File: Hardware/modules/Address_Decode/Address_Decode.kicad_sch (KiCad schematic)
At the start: 28 parts, among them J1 Bus_PCI_6502, J2 Clock_Sel, J3 Conn_01x08, SW1 Manual_Clock, U1 74HC14, U2 74HC00, U3 74LS20, U4 DS1501YZ, U5 74LS393, U6 74HC138, U7 74HC688, X1 8MHz, Y1 G33270007

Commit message: Big Hardware Update
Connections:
- net PORT_144: now also U2.9
- net PORT_160: no longer U2.9
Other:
- note added: "Address PORT 144@16 -> BF90 - BF9F"
- note removed: "Address PORT 160@16 -> BFA0 - BFAF"
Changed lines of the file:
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@@
 		)
 	)
-	(text "Address PORT 160@16\n-> BFA0 - BFAF"
+	(text "Address PORT 144@16\n-> BF90 - BF9F"
 		(exclude_from_sim no)
 		(at 178.562 28.194 0)
@@
 	)
 	(label "PORT_144"
+		(at 201.93 73.66 180)
+		(fields_autoplaced yes)
+		(effects
+			(font
+				(size 1.27 1.27)
+			)
+			(justify right bottom)
+		)
+	)
+	(label "PORT_144"
 		(at 199.39 106.68 0)
 		(fields_autoplaced yes)
@@
 		)
 	)
-	(label "PORT_160"
-		(at 201.93 73.66 180)
-		(fields_autoplaced yes)
-		(effects
-			(font
-				(size 1.27 1.27)
-			)
-			(justify right bottom)
-		)
-	)

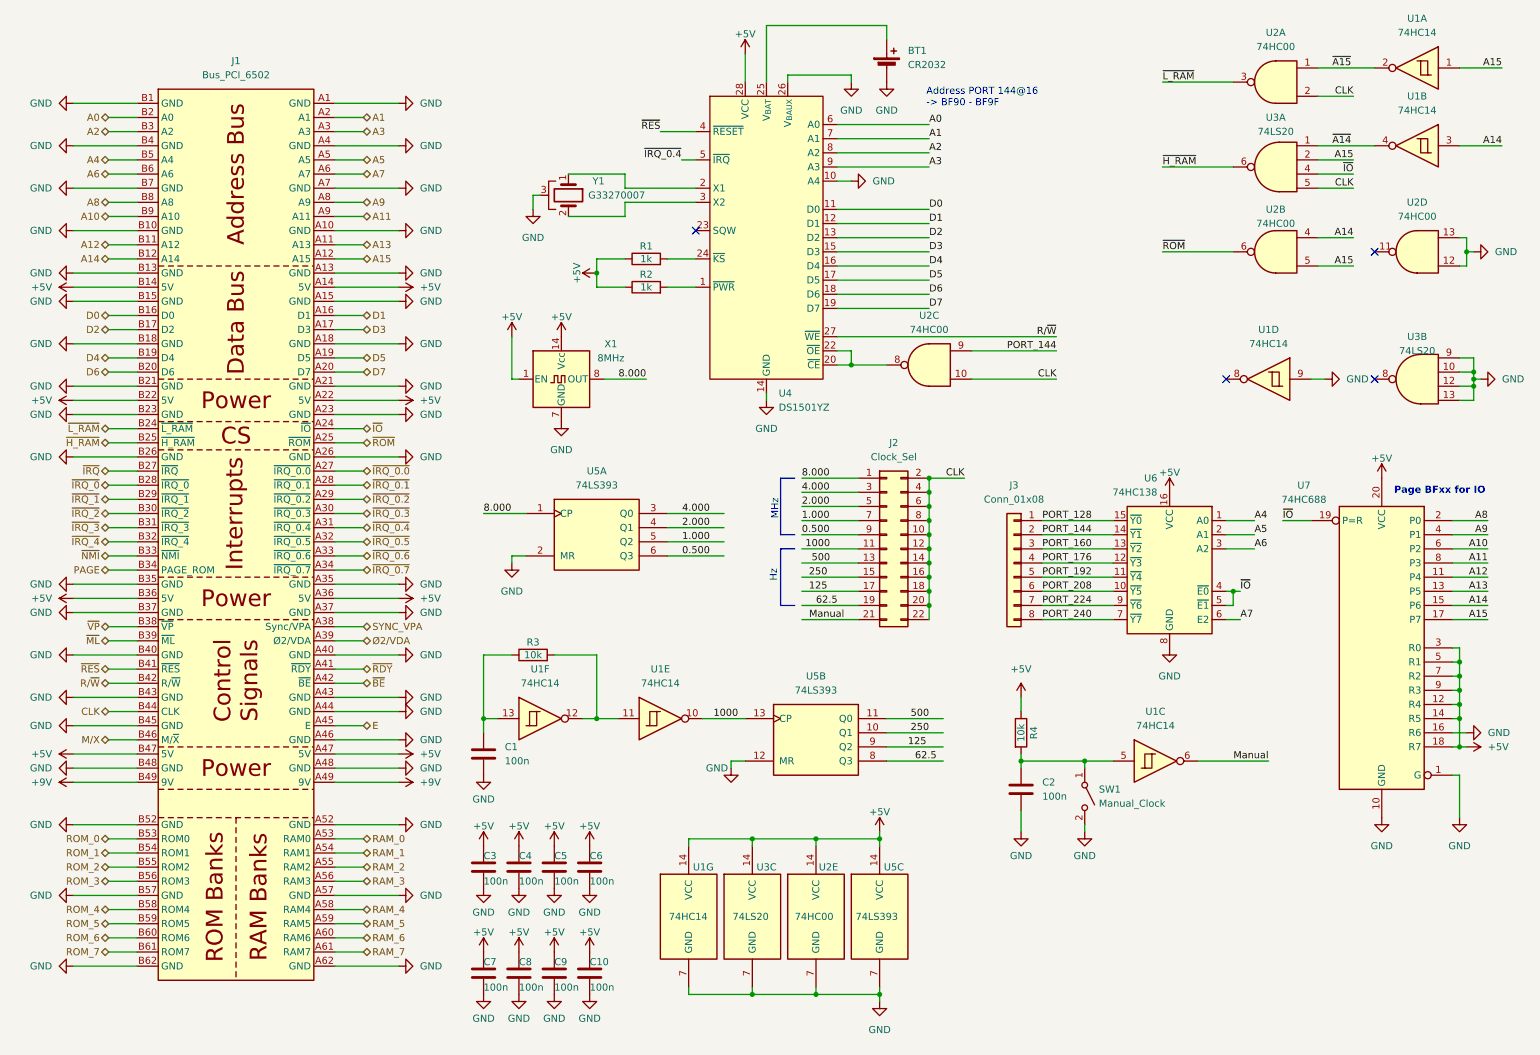
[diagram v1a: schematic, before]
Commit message: Hardware Update Add MyCPU VGA Module Beautify all Schematics minor Error corrections Readme Update
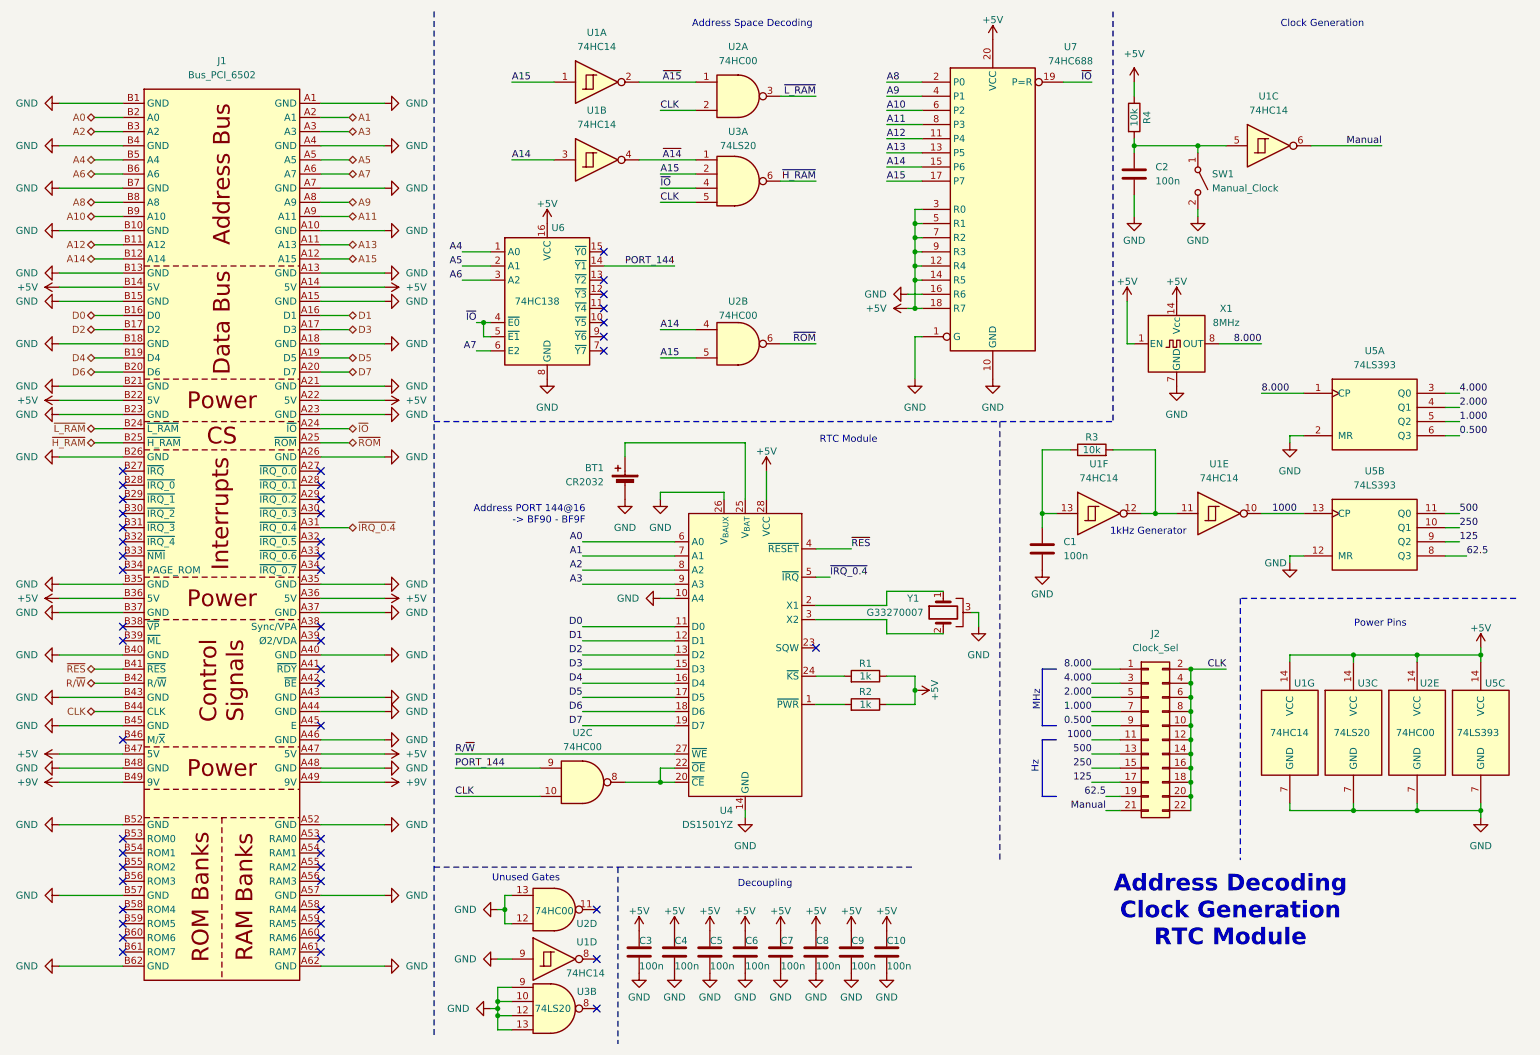
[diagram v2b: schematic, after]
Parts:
- removed J3: Conn_01x08, Connector_PinHeader_2.54mm:PinHeader_1x08_P2.54mm_Vertical, symbol Connector_Generic:Conn_01x08
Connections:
- net E: no longer names the net of J1.A45 (E)
- net M/X: no longer names the net of J1.B46 (M/~{X})
- net PAGE: no longer names the net of J1.B34 (PAGE_ROM)
- net PORT_128: no longer names the net of U6.15 (~{Y0})
- net PORT_160: no longer names the net of U6.13 (~{Y2})
- net PORT_176: no longer names the net of U6.12 (~{Y3})
- net PORT_192: no longer names the net of U6.11 (~{Y4})
- net PORT_208: no longer names the net of U6.10 (~{Y5})
- net PORT_224: no longer names the net of U6.9 (~{Y6})
- net PORT_240: no longer names the net of U6.7 (~{Y7})
- net RAM_0: no longer names the net of J1.A53 (RAM0)
- net RAM_1: no longer names the net of J1.A54 (RAM1)
- net RAM_2: no longer names the net of J1.A55 (RAM2)
- net RAM_3: no longer names the net of J1.A56 (RAM3)
- net RAM_4: no longer names the net of J1.A58 (RAM4)
- net RAM_5: no longer names the net of J1.A59 (RAM5)
- net RAM_6: no longer names the net of J1.A60 (RAM6)
- net RAM_7: no longer names the net of J1.A61 (RAM7)
- net ROM_0: no longer names the net of J1.B53 (ROM0)
- net ROM_1: no longer names the net of J1.B54 (ROM1)
- net ROM_2: no longer names the net of J1.B55 (ROM2)
- net ROM_3: no longer names the net of J1.B56 (ROM3)
- net ROM_4: no longer names the net of J1.B58 (ROM4)
- net ROM_5: no longer names the net of J1.B59 (ROM5)
- net ROM_6: no longer names the net of J1.B60 (ROM6)
- net ROM_7: no longer names the net of J1.B61 (ROM7)
- net SYNC_VPA: no longer names the net of J1.A38 (Sync/VPA)
- net ~{BE}: no longer names the net of J1.A42 (~{BE})
- net ~{IRQ_0.0}: no longer names the net of J1.A27 (~{IRQ_0.0})
- net ~{IRQ_0.1}: no longer names the net of J1.A28 (~{IRQ_0.1})
- net ~{IRQ_0.2}: no longer names the net of J1.A29 (~{IRQ_0.2})
- net ~{IRQ_0.3}: no longer names the net of J1.A30 (~{IRQ_0.3})
- net ~{IRQ_0.5}: no longer names the net of J1.A32 (~{IRQ_0.5})
- net ~{IRQ_0.6}: no longer names the net of J1.A33 (~{IRQ_0.6})
- net ~{IRQ_0.7}: no longer names the net of J1.A34 (~{IRQ_0.7})
- net ~{IRQ_0}: no longer names the net of J1.B28 (~{IRQ_0})
- net ~{IRQ_1}: no longer names the net of J1.B29 (~{IRQ_1})
- net ~{IRQ_2}: no longer names the net of J1.B30 (~{IRQ_2})
- net ~{IRQ_3}: no longer names the net of J1.B31 (~{IRQ_3})
- net ~{IRQ_4}: no longer names the net of J1.B32 (~{IRQ_4})
- net ~{IRQ}: no longer names the net of J1.B27 (~{IRQ})
- net ~{ML}: no longer names the net of J1.B39 (~{ML})
- net ~{NMI}: no longer names the net of J1.B33 (~{NMI})
- net ~{RDY}: no longer names the net of J1.A41 (~{RDY})
- net ~{VP}: no longer names the net of J1.B38 (~{VP})
- net Ø2/VDA: no longer names the net of J1.A39 (Ø2/VDA)
- no-connect marks 4 -> 50
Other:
- note added: "1kHz Generator"
- note added: "Address Decoding Clock Generation RTC Module"
- note added: "Address Space Decoding"
- note added: "Clock Generation"
- note added: "Decoupling"
- note added: "Power Pins"
- note added: "RTC Module"
- note added: "Unused Gates"
- note removed: "Page BFxx for IO"
- company: (none) -> Synthron
- title: (none) -> S65xx Computer System
- moved on the sheet: BT1, C1, C10, C2, C3, C4, C5, C6, C7, C8, C9, J1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

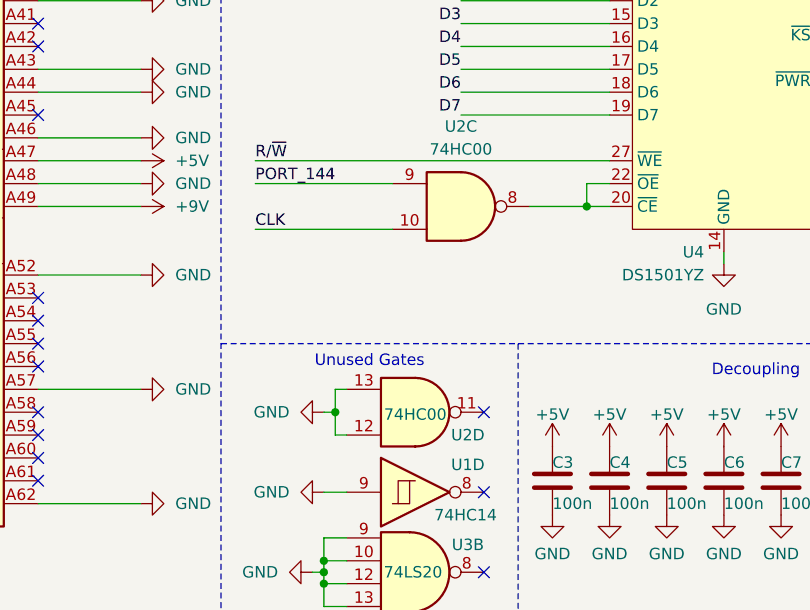
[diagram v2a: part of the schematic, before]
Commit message: Chip Select Strobe Generation Bugfix
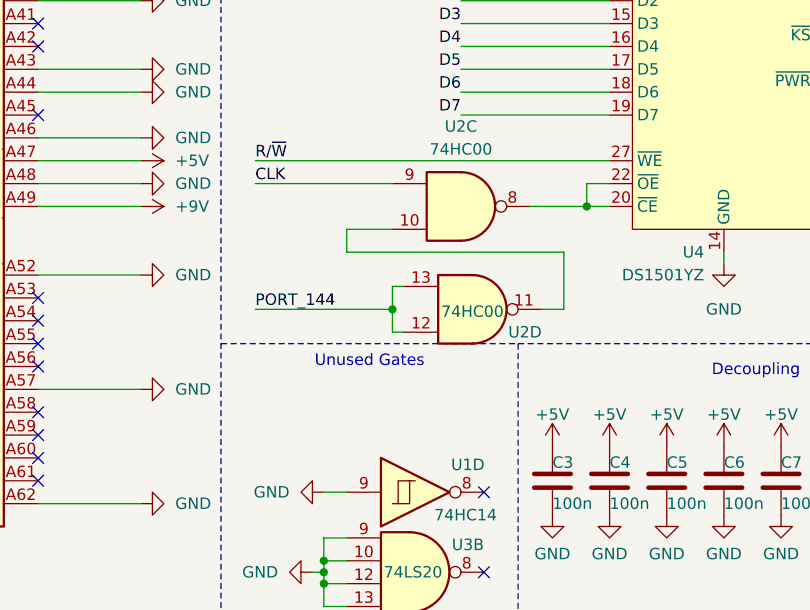
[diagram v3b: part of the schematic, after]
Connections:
- net CLK: now also U2.9; no longer U2.10
- net GND: no longer U2.12, U2.13
- net PORT_144: now also U2.12, U2.13; no longer U2.9
- net at U2.11: now also U2.10
- no-connect marks 50 -> 49
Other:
- moved on the sheet: U2D
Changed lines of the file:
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@@
 	)
 	(junction
-		(at 102.87 173.99)
+		(at 176.53 55.88)
 		(diameter 0)
 		(color 0 0 0 0)
 	)
 	(junction
-		(at 176.53 55.88)
+		(at 99.06 68.58)
 		(diameter 0)
 		(color 0 0 0 0)
 	)
 	(junction
-		(at 99.06 68.58)
+		(at 109.22 162.56)
 		(diameter 0)
 		(color 0 0 0 0)
@@
 	)
 	(no_connect
-		(at 119.38 173.99)
-	)
-	(no_connect
 		(at 120.65 73.66)
 	)
@@
 	(wire
 		(pts
-			(xy 102.87 173.99) (xy 102.87 176.53)
+			(xy 208.28 148.59) (xy 213.36 148.59)
 		)
 		(stroke
@@
 	(wire
 		(pts
-			(xy 208.28 148.59) (xy 213.36 148.59)
+			(xy 171.45 35.56) (xy 177.8 35.56)
 		)
 		(stroke
@@
 	(wire
 		(pts
-			(xy 171.45 35.56) (xy 177.8 35.56)
+			(xy 22.86 140.97) (xy 34.29 140.97)
 		)
 		(stroke
@@
 	(wire
 		(pts
-			(xy 22.86 140.97) (xy 34.29 140.97)
+			(xy 81.28 148.59) (xy 69.85 148.59)
 		)
 		(stroke
@@
 	(wire
 		(pts
-			(xy 81.28 148.59) (xy 69.85 148.59)
+			(xy 104.14 193.04) (xy 101.6 193.04)
 		)
 		(stroke
@@
 	(wire
 		(pts
-			(xy 104.14 193.04) (xy 101.6 193.04)
+			(xy 109.22 162.56) (xy 109.22 160.02)
 		)
 		(stroke
@@
 	(wire
 		(pts
+			(xy 104.14 156.21) (xy 104.14 153.67)
+		)
+		(stroke
+			(width 0)
+			(type default)
+		)
+	)
+	(wire
+		(pts
 			(xy 255.27 128.27) (xy 243.84 128.27)
 		)
@@
 	(wire
 		(pts
-			(xy 102.87 176.53) (xy 104.14 176.53)
-		)
-		(stroke
-			(width 0)
-			(type default)
-		)
-	)
-	(wire
-		(pts
 			(xy 74.93 41.91) (xy 69.85 41.91)
 		)
@@
 	(wire
 		(pts
-			(xy 102.87 171.45) (xy 102.87 173.99)
-		)
-		(stroke
-			(width 0)
-			(type default)
-		)
-	)
-	(wire
-		(pts
 			(xy 274.32 105.41) (xy 271.78 105.41)
 		)
@@
 	(wire
 		(pts
+			(xy 128.27 156.21) (xy 104.14 156.21)
+		)
+		(stroke
+			(width 0)
+			(type default)
+		)
+	)
+	(wire
+		(pts
 			(xy 226.06 138.43) (xy 226.06 140.97)
 		)
@@
 	(wire
 		(pts
+			(xy 125.73 162.56) (xy 128.27 162.56)
+		)
+		(stroke
+			(width 0)
+			(type default)
+		)
+	)
+	(wire
+		(pts
 			(xy 22.86 62.23) (xy 34.29 62.23)
 		)
@@
 	(wire
 		(pts
-			(xy 102.87 171.45) (xy 104.14 171.45)
+			(xy 171.45 43.18) (xy 177.8 43.18)
 		)
 		(stroke
@@
 	(wire
 		(pts
-			(xy 171.45 43.18) (xy 177.8 43.18)
+			(xy 226.06 130.81) (xy 226.06 133.35)
 		)
 		(stroke
@@
 	(wire
 		(pts
-			(xy 226.06 130.81) (xy 226.06 133.35)
+			(xy 22.86 59.69) (xy 34.29 59.69)
 		)
 		(stroke
@@
 	(wire
 		(pts
-			(xy 22.86 59.69) (xy 34.29 59.69)
+			(xy 74.93 74.93) (xy 69.85 74.93)
 		)
 		(stroke
@@
 	(wire
 		(pts
-			(xy 74.93 74.93) (xy 69.85 74.93)
+			(xy 137.16 39.37) (xy 127 39.37)
 		)
 		(stroke
@@
 	(wire
 		(pts
-			(xy 137.16 39.37) (xy 127 39.37)
+			(xy 110.49 165.1) (xy 109.22 165.1)
 		)
 		(stroke
@@
 	(wire
 		(pts
+			(xy 109.22 160.02) (xy 110.49 160.02)
+		)
+		(stroke
+			(width 0)
+			(type default)
+		)
+	)
+	(wire
+		(pts
 			(xy 29.21 69.85) (xy 34.29 69.85)
 		)
@@
 	(wire
 		(pts
-			(xy 102.87 173.99) (xy 101.6 173.99)
+			(xy 176.53 48.26) (xy 176.53 50.8)
 		)
 		(stroke
@@
 	(wire
 		(pts
-			(xy 176.53 48.26) (xy 176.53 50.8)
+			(xy 128.27 162.56) (xy 128.27 156.21)
 		)
 		(stroke
@@
 	(wire
 		(pts
-			(xy 109.22 148.59) (xy 93.98 148.59)
+			(xy 109.22 162.56) (xy 93.98 162.56)
 		)
 		(stroke
@@
 	(wire
 		(pts
-			(xy 93.98 153.67) (xy 109.22 153.67)
+			(xy 93.98 148.59) (xy 109.22 148.59)
 		)
 		(stroke
@@
 	(wire
 		(pts
+			(xy 109.22 165.1) (xy 109.22 162.56)
+		)
+		(stroke
+			(width 0)
+			(type default)
+		)
+	)
+	(wire
+		(pts
+			(xy 104.14 153.67) (xy 109.22 153.67)
+		)
+		(stroke
+			(width 0)
+			(type default)
+		)
+	)
+	(wire
+		(pts
 			(xy 29.21 46.99) (xy 34.29 46.99)
 		)
@@
 	)
 	(label "CLK"
-		(at 93.98 153.67 0)
+		(at 93.98 148.59 0)
 		(fields_autoplaced yes)
 		(effects
@@
 	)
 	(label "PORT_144"
-		(at 93.98 148.59 0)
+		(at 93.98 162.56 0)
 		(fields_autoplaced yes)
 		(effects
@@
 	(symbol
 		(lib_id "74xx:74HC00")
-		(at 111.76 173.99 0)
+		(at 118.11 162.56 0)
 		(mirror x)
 		(unit 4)
@@
 		(dnp no)
 		(property "Reference" "U2"
-			(at 117.602 176.53 0)
+			(at 123.952 165.1 0)
 			(effects
 				(font
@@
 		)
 		(property "Value" "74HC00"
-			(at 111.76 174.244 0)
+			(at 118.11 162.814 0)
 			(effects
 				(font
@@
 		)
 		(property "Footprint" "Package_DIP:DIP-14_W7.62mm_LongPads"
-			(at 111.76 173.99 0)
+			(at 118.11 162.56 0)
 			(effects
 				(font
@@
 		)
 		(property "Datasheet" "http://www.ti.com/lit/gpn/sn74hc00"
-			(at 111.76 173.99 0)
+			(at 118.11 162.56 0)
 			(effects
 				(font
@@
 		)
 		(property "Description" "quad 2-input NAND gate"
-			(at 111.76 173.99 0)
+			(at 118.11 162.56 0)
 			(effects
 				(font
@@
 					(unit 1)
 				)
-			)
-		)
-	)
-	(symbol
-		(lib_id "power:GND")
-		(at 101.6 173.99 270)
-		(mirror x)
-		(unit 1)
-		(exclude_from_sim no)
-		(in_bom yes)
-		(on_board yes)
-		(dnp no)
-		(fields_autoplaced yes)
-		(property "Reference" "#PWR014"
-			(at 95.25 173.99 0)
-			(effects
-				(font
-					(size 1.27 1.27)
-				)
-				(hide yes)
-			)
-		)
-		(property "Value" "GND"
-			(at 97.79 173.9899 90)
-			(effects
-				(font
-					(size 1.27 1.27)
-				)
-				(justify right)
-			)
-		)
-		(property "Footprint" ""
-			(at 101.6 173.99 0)
-			(effects
-				(font
-					(size 1.27 1.27)
-				)
-				(hide yes)
-			)
-		)
-		(property "Datasheet" ""
-			(at 101.6 173.99 0)
-			(effects
-				(font
-					(size 1.27 1.27)
-				)
-				(hide yes)
-			)
-		)
-		(property "Description" "Power symbol creates a global label with name \"GND\" , ground"
-			(at 101.6 173.99 0)
-			(effects
-				(font
-					(size 1.27 1.27)
-				)
-				(hide yes)
-			)
-		)
-		(pin "1"
-		)
-		(instances
-			(project "Address_Decode"
-				(path "/a8f3be35-d595-4d09-a3be-a54adbc9e0af"
-					(reference "#PWR014")
-					(unit 1)
-				)

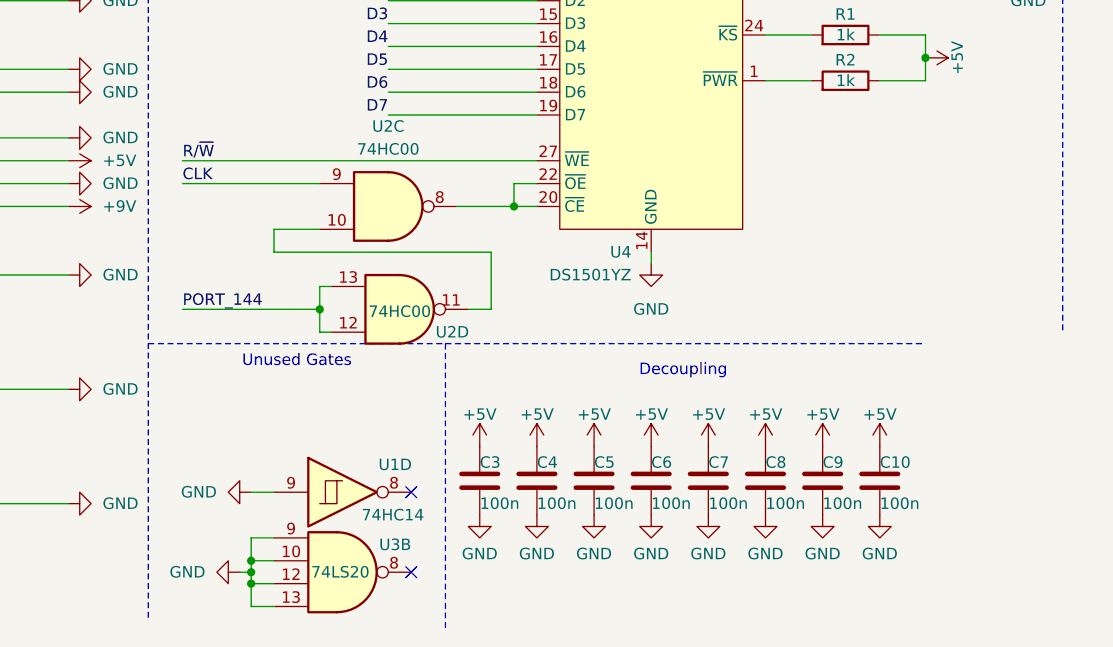
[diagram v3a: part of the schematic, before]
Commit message: Hardware Review Pt. 1 fix Address Decoding for Strobe Generators add bulk capacitance to every board fix wiring of Prototyping Board
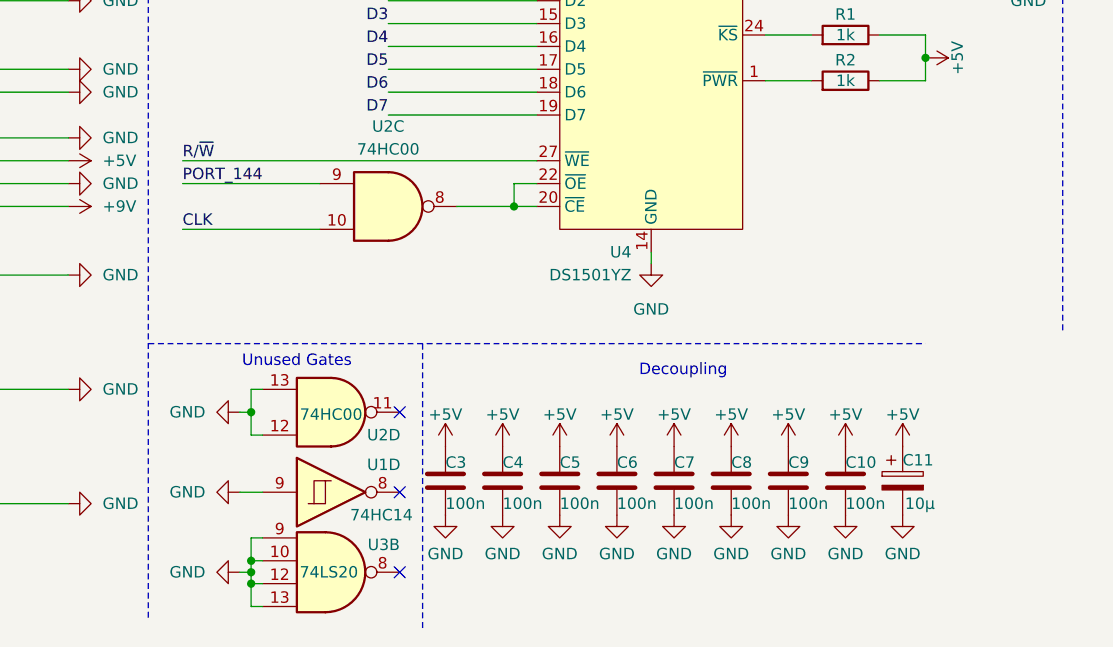
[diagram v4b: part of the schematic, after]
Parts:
- added C11: 10µ, Capacitor_THT:CP_Radial_D5.0mm_P2.50mm, symbol Device:C_Polarized
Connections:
- net +5V: now also C11.1
- net CLK: now also U2.10; no longer U2.9
- net GND: now also U2.12, U2.13, C11.2
- net PORT_144: now also U2.9; no longer U2.12, U2.13
- net at U2.11: no longer U2.10
- no-connect marks 49 -> 50
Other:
- moved on the sheet: C10, C3, C4, C5, C6, C7, C8, C9, U1D, U2D, U3B
